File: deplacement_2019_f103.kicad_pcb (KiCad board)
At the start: 2 copper layers, 50.8 x 85.1 mm, 24 parts, among them J1 Alim logique, J2 Connecteur Gauche, J3 Connecteur Droit, J4 Conn_01x05, J5 Conn_01x05, J6 PWM output, J7 PWM output, J8 Liaison serie, Q1 PMF370XN, Q2 PMF370XN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

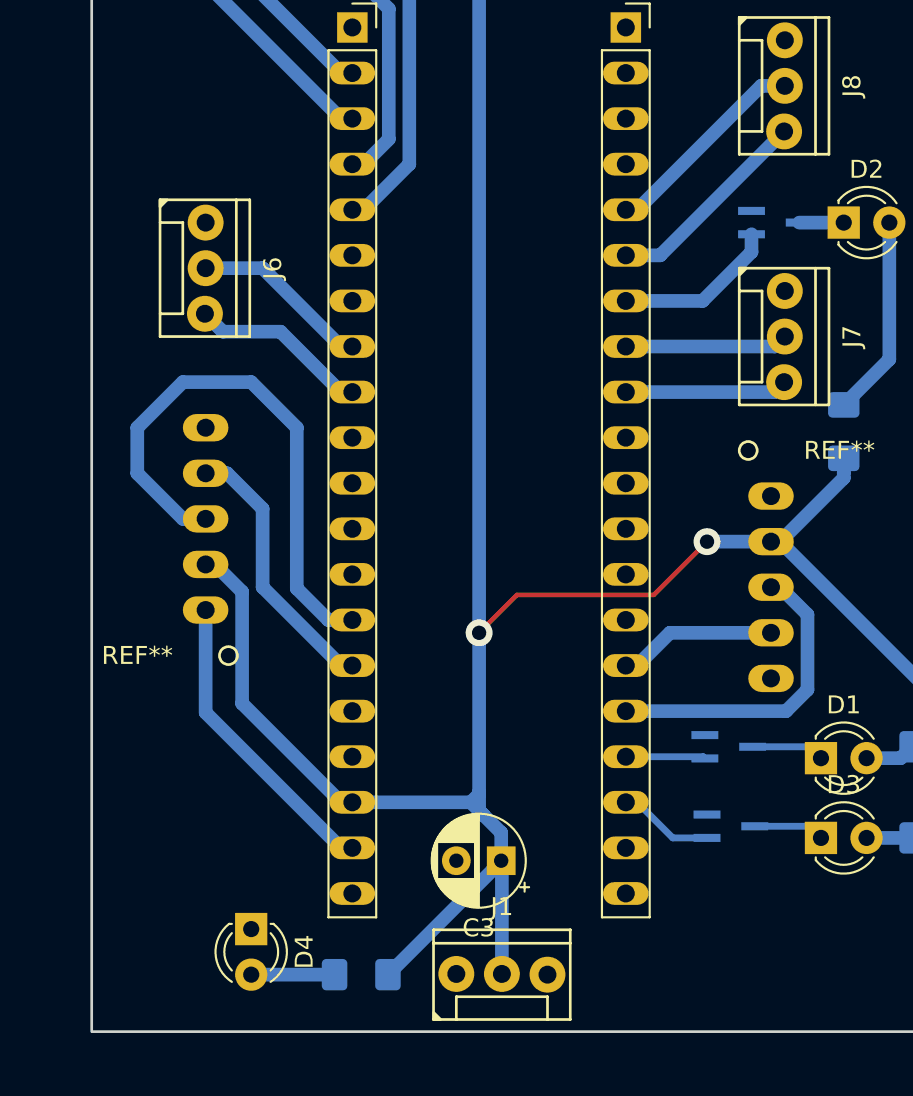
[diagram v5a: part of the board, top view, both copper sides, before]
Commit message: Added testpoints
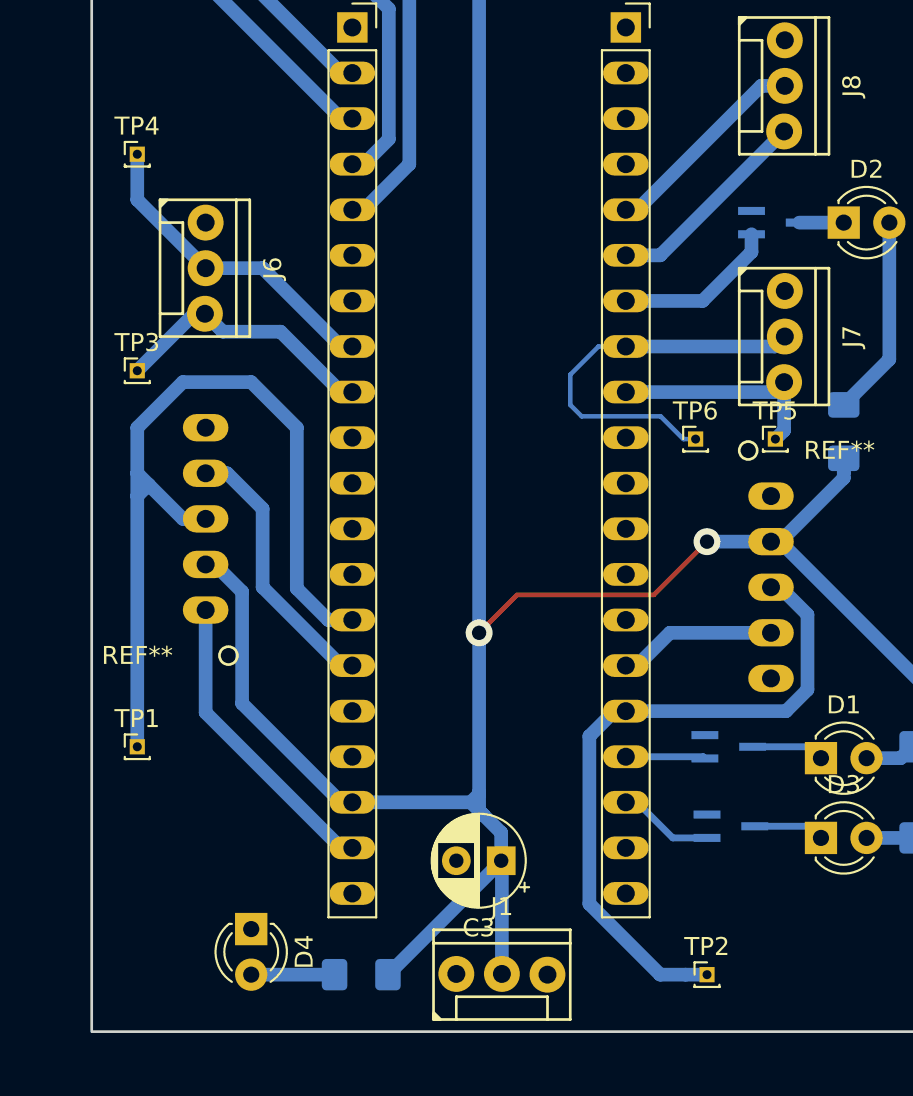
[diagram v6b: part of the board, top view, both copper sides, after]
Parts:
- added TP1: TestPoint_Probe, Connector_PinHeader_1.00mm:PinHeader_1x01_P1.00mm_Vertical, F.Cu at (129.5, 115.6)
- added TP2: TestPoint_Probe, Connector_PinHeader_1.00mm:PinHeader_1x01_P1.00mm_Vertical, F.Cu at (161.3, 128.3)
- added TP3: TestPoint_Probe, Connector_PinHeader_1.00mm:PinHeader_1x01_P1.00mm_Vertical, F.Cu at (129.5, 94.6)
- added TP4: TestPoint_Probe, Connector_PinHeader_1.00mm:PinHeader_1x01_P1.00mm_Vertical, F.Cu at (129.5, 82.5)
- added TP5: TestPoint_Probe, Connector_PinHeader_1.00mm:PinHeader_1x01_P1.00mm_Vertical, F.Cu at (165.1, 98.4)
- added TP6: TestPoint_Probe, Connector_PinHeader_1.00mm:PinHeader_1x01_P1.00mm_Vertical, F.Cu at (160.7, 98.4)
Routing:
- net /qei_right_A: track 17.5 -> 37.6 mm
- net /qei_left_A: track 31.9 -> 48.0 mm
- net /motor_right_PWM: track 9.09 -> 22.3 mm
- net /motor_left_PWM: track 9.98 -> 17.9 mm
- net /motor_left_direction: track 10.0 -> 15.1 mm
- net /motor_right_direction: track 9.05 -> 12.4 mm

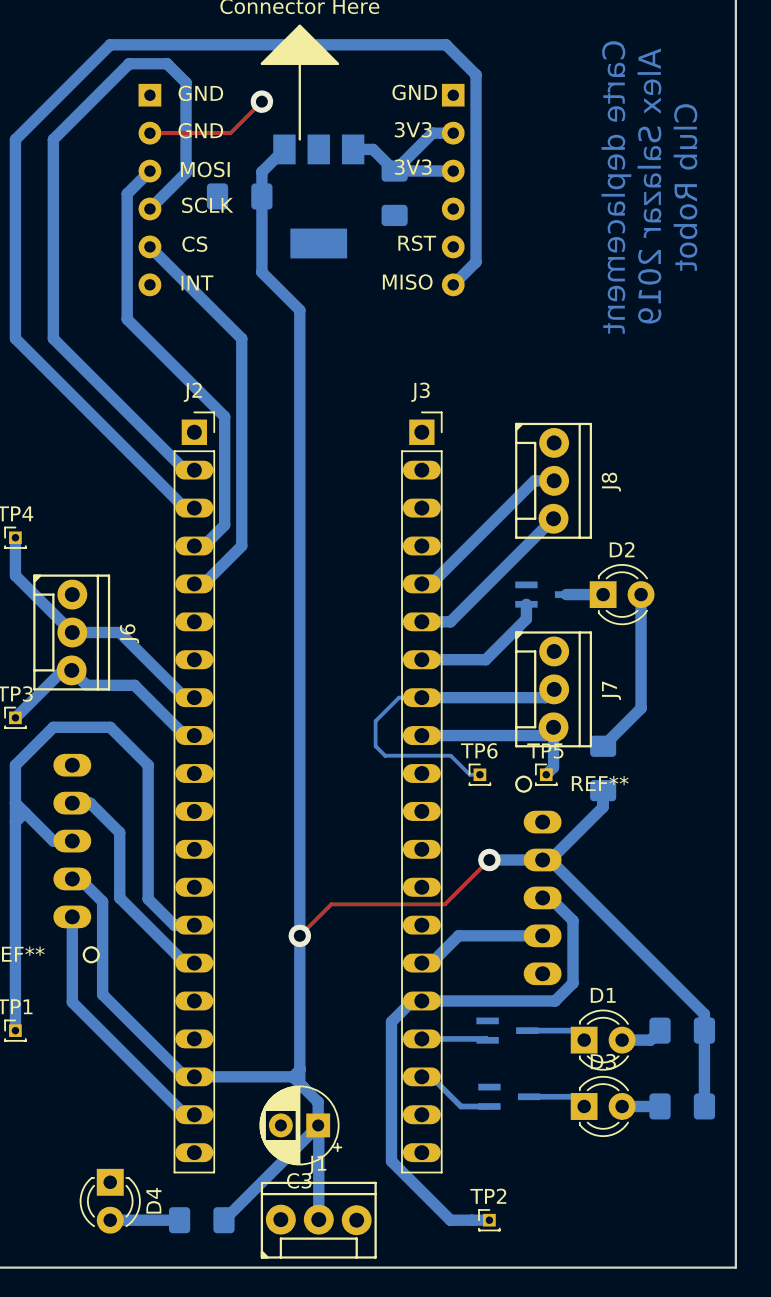
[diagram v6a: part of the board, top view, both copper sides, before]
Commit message: removed an floating wire
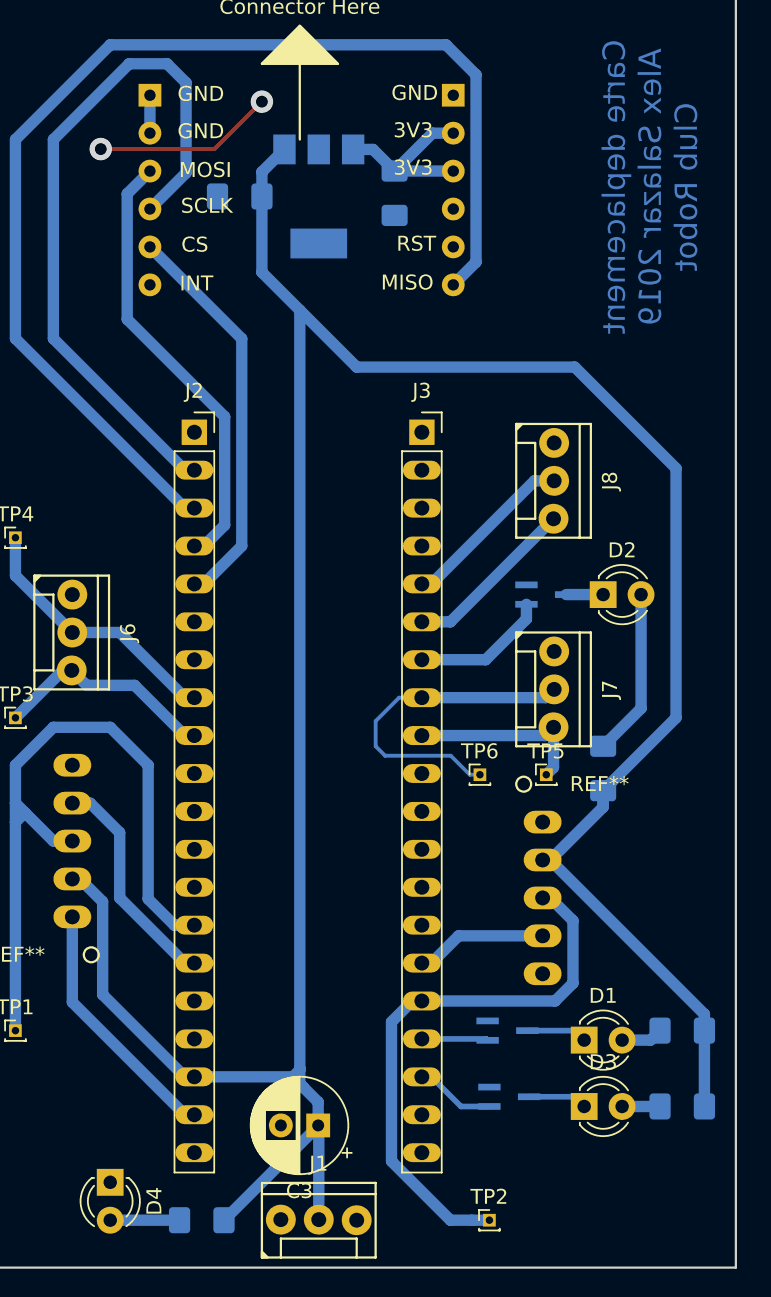
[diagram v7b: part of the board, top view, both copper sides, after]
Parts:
- C3: footprint Capacitor_THT:CP_Radial_D5.0mm_P2.50mm -> Capacitor_THT:CP_Radial_D6.3mm_P2.50mm
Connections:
- J3 pad 12: Net-(J3-Pad12) -> GND
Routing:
- net +5V: track 154.3 -> 189.1 mm, vias 2 -> 0
- net GND: track 25.4 -> 31.7 mm, vias 1 -> 2

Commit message: place footprints
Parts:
- J4, J5: footprint @Robot:HE14-5_horizontal -> @Robot:HE14-5-straight
- moved R1 84.7 mm to (100.0, 74.8), turned to 0 degrees
- moved R3 84.6 mm to (100.0, 80.0), turned to 0 degrees
- moved D1 73.5 mm to (106.9, 74.9), turned to 180 degrees
- moved D3 73.1 mm to (106.9, 80.0), turned to 180 degrees
- moved R2 70.1 mm to (100.0, 85.1), turned to 0 degrees
- moved Q1 65.5 mm to (111.1, 74.9), turned to 180 degrees
- moved Q3 65.2 mm to (111.1, 80.0), turned to 180 degrees
- moved D2 62.1 mm to (106.9, 85.1), turned to 180 degrees
- moved Q2 54.0 mm to (111.1, 85.1), turned to 180 degrees
- moved J1 38.9 mm to (111.3, 121.9), turned to 270 degrees
- moved J5 33.1 mm to (137.8, 116.2), turned to 90 degrees
- moved J7 29.5 mm to (137.6, 99.2), turned to 90 degrees
- moved TP4 29.4 mm to (102.2, 93.3)
- moved C1 28.5 mm to (116.2, 57.1), turned to 90 degrees
- moved U1 28.4 mm to (121.5, 62.2)
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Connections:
- J2 pad 1: Net-(J2-Pad1) -> /led_hardfault
- J2 pad 2: /SCLK -> Net-(J2-Pad2)
- J2 pad 3: /MISO -> /led_feedback
- J2 pad 4: /MOSI -> Net-(J2-Pad4)
- J2 pad 5: /CS -> /led_communication
- J3 pad 10: Net-(J3-Pad10) -> /MISO
- J3 pad 11: Net-(J3-Pad11) -> /SCLK
- J3 pad 13: Net-(J3-Pad13) -> /motor_right_direction
- J3 pad 14: Net-(J3-Pad14) -> /motor_right_PWM
- J3 pad 17: /led_hardfault -> Net-(J3-Pad17)
- J3 pad 18: /led_feedback -> Net-(J3-Pad18)
- J3 pad 7: /led_communication -> Net-(J3-Pad7)
- J3 pad 8: /motor_right_PWM -> /CS
- J3 pad 9: /motor_right_direction -> /MOSI
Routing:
- net +5V: track 189.1 -> 3.78 mm
- net /MISO: track 79.0 -> 0.00 mm
- net /qei_left_A: track 48.0 -> 0.00 mm
- net /SCLK: track 47.4 -> 0.00 mm
- net /qei_right_A: track 37.6 -> 0.00 mm
- net GND: track 31.7 -> 0.00 mm, vias 2 -> 0
- net /MOSI: track 29.7 -> 0.00 mm
- net /CS: track 26.8 -> 0.00 mm
- net /motor_right_PWM: track 22.3 -> 0.00 mm
- net /motor_left_PWM: track 17.9 -> 0.00 mm
- net /motor_left_direction: track 15.1 -> 0.00 mm
- net /qei_left_B: track 14.5 -> 0.00 mm
- net /motor_right_direction: track 12.4 -> 0.00 mm
- net /RX: track 11.7 -> 0.00 mm
- net /TX: track 11.7 -> 0.00 mm
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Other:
- board outline removed
- net class Default: trace_width 0.762 -> 0.381; via_dia 1.5 -> 0.8; via_drill 0.8 -> 0.4
- board text removed: "Carte deplacement Alex Salazar 2019 Club Robot"
